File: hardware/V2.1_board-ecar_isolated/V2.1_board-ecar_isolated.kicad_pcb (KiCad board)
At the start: 2 copper layers, 160 x 100 mm, 99 parts, among them IC1 ATMEGA8A-P, J1 2x BATT IN, J10 24V, J11 18V, J12 5V, J13 Analog-in-2 0-5V, J14 IGBT [GND, Gate], J15 Analog-in-3 - 30to5 (batt), J17 2x Switch (to 5V), J18 Relay contacts [NO, COM, NC], J19 2x 5V, J2 ST 2x GND, J20 ADC Battery, J21 ADC reserve, J22 ADC Gas-pedal, J23 2x 24V filtered, J24 Fan [GND-supp, Diode, Mosfet], J3 2x 24V filtered, J4 ST 2x GND, J5 PWM-Signal, J6 LED 3,2V 20mA [-, +], J7 Gas Pedal, J8 Gate, J9 BATT, K1 LEG-5, P1 ISP, Q1 BC547, Q2 IRFZ24N, Q3 BC547, U1 LM7818CT, U2 LM2576T-5, U3 TC429

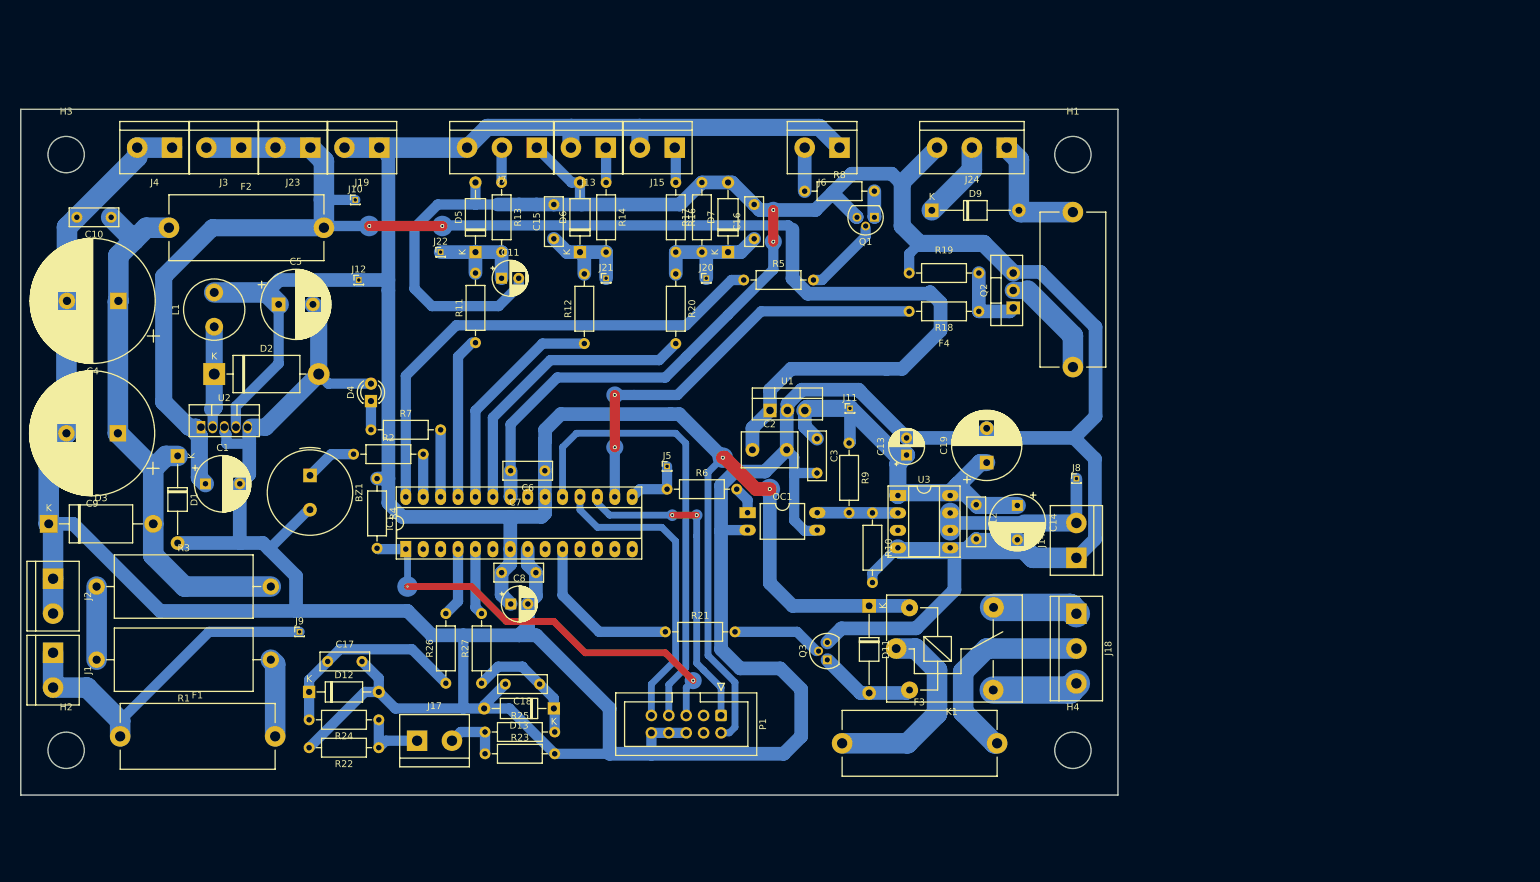
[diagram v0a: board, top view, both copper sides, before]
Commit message: pcb: small additions, begin footprint placment
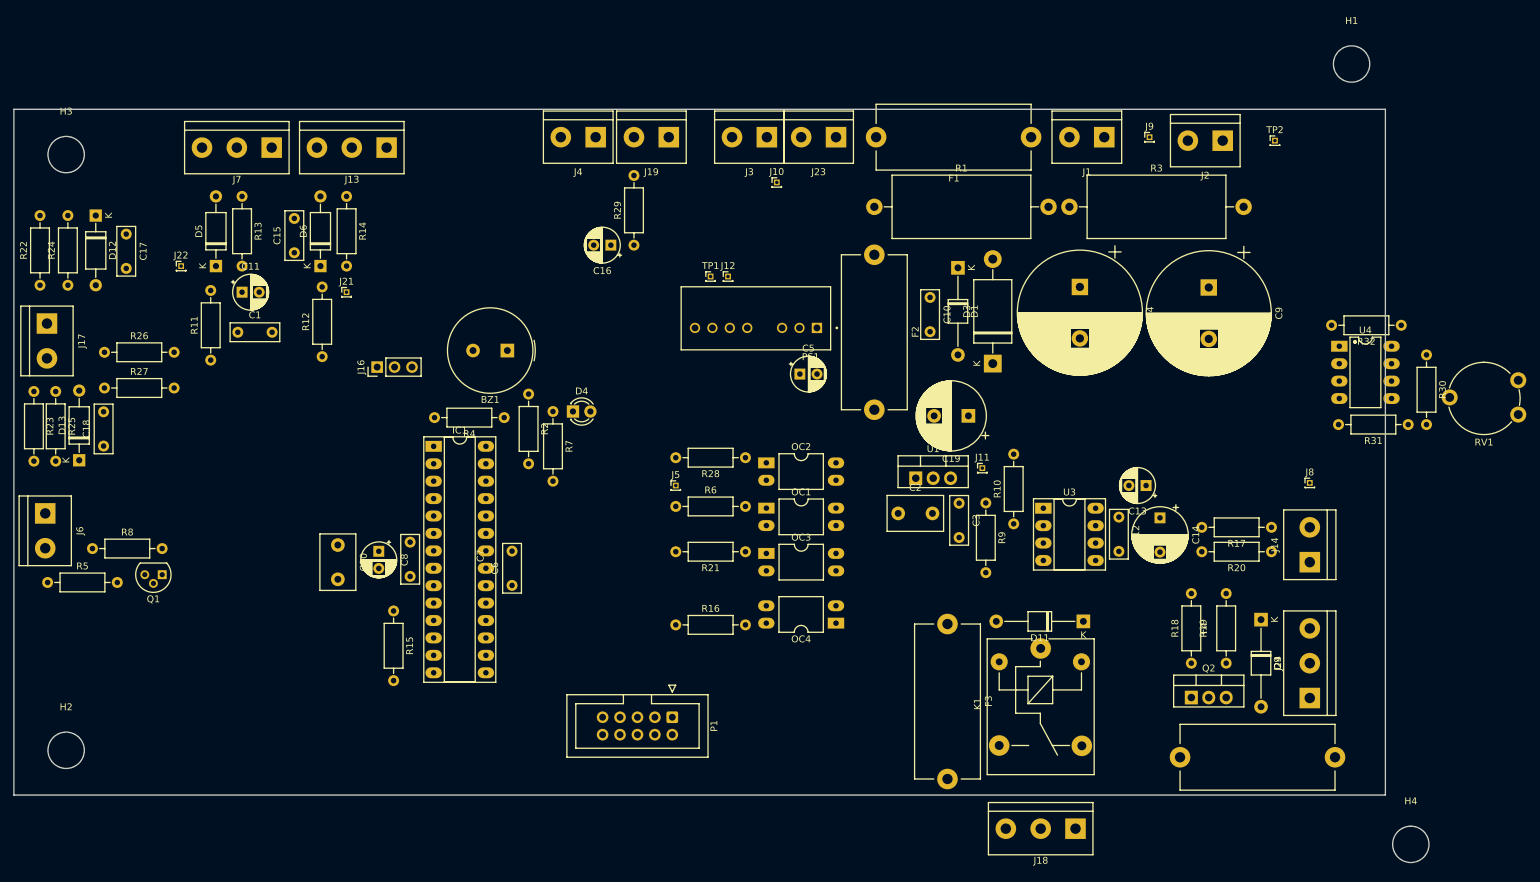
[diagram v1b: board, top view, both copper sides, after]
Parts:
- removed D2: 1N5822, Diode_THT:D_DO-201AD_P15.24mm_Horizontal
- removed D7: 5V1, Diode_THT:D_A-405_P10.16mm_Horizontal
- removed J15: Analog-in-3 - 30to5 (batt), TerminalBlock:TerminalBlock_bornier-2_P5.08mm
- removed J20: ADC Battery, Connector_PinHeader_1.00mm:PinHeader_1x01_P1.00mm_Vertical
- removed L1: 100u, Inductor_THT:L_Radial_D8.7mm_P5.00mm_Fastron_07HCP
- removed Q3: BC547, Package_TO_SOT_THT:TO-92L
- removed U2: LM2576T-5, Package_TO_SOT_THT:TO-220-5_Vertical
- added C20: 330nF, Capacitor_THT:C_Disc_D8.0mm_W5.0mm_P5.00mm, F.Cu at (47.2, 63.5)
- added J16: UART [TX, RX, GND], Connector_PinHeader_2.54mm:PinHeader_1x03_P2.54mm_Vertical, F.Cu at (53.0, 37.6)
- added OC2: LTV-817, Package_DIP:DIP-4_W10.16mm_LongPads, F.Cu at (109.7, 51.6)
- added OC3: LTV-817, Package_DIP:DIP-4_W10.16mm_LongPads, F.Cu at (109.7, 64.8)
- added OC4: LTV-817, Package_DIP:DIP-4_W10.16mm_LongPads, F.Cu at (119.9, 74.9)
- added PS1: RSO-2405S, RSO-2405S:CONV_RSO-2405S, F.Cu at (108.2, 30.5)
- added R15: 330, Resistor_THT:R_Axial_DIN0207_L6.3mm_D2.5mm_P10.16mm_Horizontal, F.Cu at (55.4, 73.2)
- added R28: 200, Resistor_THT:R_Axial_DIN0207_L6.3mm_D2.5mm_P10.16mm_Horizontal, F.Cu at (106.7, 50.8)
- added R29: 20, Resistor_THT:R_Axial_DIN0207_L6.3mm_D2.5mm_P10.16mm_Horizontal, F.Cu at (90.4, 19.8)
- added R30: 150k, Resistor_THT:R_Axial_DIN0207_L6.3mm_D2.5mm_P10.16mm_Horizontal, F.Cu at (206.0, 35.8)
- added R31: 100k, Resistor_THT:R_Axial_DIN0207_L6.3mm_D2.5mm_P10.16mm_Horizontal, F.Cu at (203.3, 46.0)
- added R32: 1k, Resistor_THT:R_Axial_DIN0207_L6.3mm_D2.5mm_P10.16mm_Horizontal, F.Cu at (202.3, 31.5)
- added RV1: 500k, Potentiometer_THT:Potentiometer_Piher_PT-10-V10_Vertical, F.Cu at (219.4, 39.5)
- added TP1: GNDD, Connector_PinHeader_1.00mm:PinHeader_1x01_P1.00mm_Vertical, F.Cu at (101.6, 24.4)
- added TP2: GND-power, Connector_PinHeader_1.00mm:PinHeader_1x01_P1.00mm_Vertical, F.Cu at (183.9, 4.57)
- added U4: LM358N, Package_DIP_AKL:DIP-8_W7.62mm_LongPads, F.Cu at (193.3, 34.6)
- C1: value 100u -> 100n; footprint Capacitor_THT:CP_Radial_D8.0mm_P5.00mm -> Capacitor_THT:C_Disc_D7.0mm_W2.5mm_P5.00mm
- C16: value 100n -> 10uf; footprint Capacitor_THT:C_Disc_D7.0mm_W2.5mm_P5.00mm -> Capacitor_THT:CP_Radial_D5.0mm_P2.50mm
- C5: value 1000u -> 10uf; footprint Capacitor_THT:CP_Radial_D10.0mm_P5.00mm -> Capacitor_THT:CP_Radial_D5.0mm_P2.50mm
- J13: value Analog-in-2 0-5V -> ADC reserve; footprint TerminalBlock:TerminalBlock_bornier-2_P5.08mm -> TerminalBlock:TerminalBlock_bornier-3_P5.08mm
- J19: value 2x 5V -> 5V, 5V-decoupled
- J2: value ST 2x GND -> ST 2x GND power
- J4: value ST 2x GND -> ST 2x GND 5V
- K1: value LEG-5 -> 24V relay
- R16: value 100k -> 10k
- R17: value 22k -> 0
- R18: value 1k -> 10k
- R19: value 22k -> 10k
- R20: value 2k2 -> nopop
- R21: value 470 -> 200
- R6: value 320 -> 200
- moved J2 182.1 mm to (176.3, 4.57), turned to 180 degrees
- moved J1 170.7 mm to (159.0, 4.06), turned to 180 degrees
- moved C9 160.5 mm to (174.2, 26.0), turned to -90 degrees
- moved F1 159.0 mm to (148.3, 4.06), turned to 180 degrees
- moved R3 152.3 mm to (153.9, 14.2)
- moved J9 143.4 mm to (165.6, 4.06)
- moved C4 140.2 mm to (155.4, 25.9), turned to -90 degrees
- moved D3 139.6 mm to (142.7, 37.1), turned to 90 degrees
- moved J6 127.5 mm to (4.57, 58.9), turned to -90 degrees
- moved C10 120.0 mm to (133.6, 27.4), turned to -90 degrees
- moved D1 117.1 mm to (137.7, 23.1)
- moved Q1 116.2 mm to (21.6, 67.9)
- moved R8 116.2 mm to (11.5, 64.1)
- moved R5 110.7 mm to (4.92, 69.0)
- moved R1 110.0 mm to (125.5, 14.2), turned to 0 degrees
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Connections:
- C1 pad 1: +24V filtered -> Net-(D5-K)
- C10 pad 2: GND -> GNDPWR
- C12 pad 2: GND -> GNDPWR
- C13 pad 2: GND -> GNDPWR
- C14 pad 2: GND -> GNDPWR
- C16 pad 1: Net-(D7-K) -> +5V
- C19 pad 2: GND -> GNDPWR
- C2 pad 2: GND -> GNDPWR
- C3 pad 2: GND -> GNDPWR
- C4 pad 2: GND -> GNDPWR
- C5 pad 1: +5V -> +24V filtered
- C5 pad 2: GND -> GNDPWR
- C9 pad 2: GND -> GNDPWR
- D1 pad 2: GND -> GNDPWR
- D11 pad 1: +5V -> +24V filtered
- D3 pad 1: GND -> GNDPWR
- IC1 pad 2: unconnected-(IC1-(RXD)PD0-Pad2) -> /UART_RX
- IC1 pad 23: /analog2 (30V Batt) -> /battery-threshold
- IC1 pad 3: unconnected-(IC1-(TXD)PD1-Pad3) -> /UART_TX
- IC1 pad 9: unconnected-(IC1-PB6(XTAL1/TOSC1)-Pad9) -> Net-(IC1-PB6(XTAL1/TOSC1))
- J13 pad 1: Net-(J13-Pin_1) -> GND
- J13 pad 2: +5V -> Net-(J13-Pin_2)
- J14 pad 1: GND -> GNDPWR
- J19 pad 2: +5V -> Net-(J19-Pin_2)
- J2 pad 1: GND -> GNDPWR
- J2 pad 2: GND -> GNDPWR
- J24 pad 3: GND -> GNDPWR
- K1 pad 5: +5V -> +24V filtered
- OC1 pad 3: GND -> GNDPWR
- P1 pad 4: unconnected-(P1-Pad4) -> GND
- Q2 pad 3: GND -> GNDPWR
- R10 pad 2: GND -> GNDPWR
- R14 pad 1: Net-(J13-Pin_1) -> Net-(J13-Pin_2)
- R16 pad 1: Net-(J15-Pin_1) -> +5V
- R16 pad 2: Net-(D7-K) -> /battery-threshold
- R17 pad 1: Net-(D7-K) -> Net-(J14-Pin_2)
- R17 pad 2: GND -> Net-(R17-Pad2)
- R18 pad 2: /Mosfet (fan) -> +24V filtered
- R19 pad 1: GND -> GNDPWR
- R20 pad 1: Net-(D7-K) -> Net-(J14-Pin_2)
- R20 pad 2: /analog2 (30V Batt) -> Net-(R17-Pad2)
- R21 pad 1: /Relay (light) -> Net-(OC3-Pad1)
- R21 pad 2: Net-(Q3-B) -> /Relay (light)
- U1 pad 2: GND -> GNDPWR
- U3 pad 4: GND -> GNDPWR
- U3 pad 5: GND -> GNDPWR
- U3 pad 6: Net-(J14-Pin_2) -> Net-(R17-Pad2)
- U3 pad 7: Net-(J14-Pin_2) -> Net-(R17-Pad2)
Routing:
- net GND: track 888.8 -> 0.00 mm, vias 2 -> 0
- net +5V: track 353.0 -> 0.00 mm, vias 2 -> 0
- net +24V filtered: track 233.3 -> 0.00 mm, vias 2 -> 0
- net Net-(D1-K): track 83.0 -> 0.00 mm
- net /LED-ext: track 72.7 -> 0.00 mm
- net +18V: track 69.5 -> 0.00 mm
- net /SCK: track 67.4 -> 0.00 mm
- net /Mosfet (fan): track 62.8 -> 0.00 mm, vias 2 -> 0
- net /RESET: track 62.6 -> 0.00 mm, vias 2 -> 0
- net +BATT: track 50.7 -> 0.00 mm
- net /MOSI: track 46.8 -> 0.00 mm, vias 2 -> 0
- net /MISO: track 44.6 -> 0.00 mm
- net /analog2 (30V Batt): track 42.7 -> 0.00 mm
- net /analog1: track 32.5 -> 0.00 mm
- net Net-(J18-Pin_2): track 30.6 -> 0.00 mm
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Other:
- board size 160 x 100 mm -> 200 x 100 mm
- board text removed: "Analog_0-30V (Pin-23/PC0) 5V(out), 24V(in)"

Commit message: pcb: optimize placement, assignment
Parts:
- removed F2: 500mA, Fuse:Fuseholder_Cylinder-5x20mm_Stelvio-Kontek_PTF78_Horizontal_Open
- removed J22: ADC Gas-pedal, Connector_PinHeader_1.00mm:PinHeader_1x01_P1.00mm_Vertical
- removed J3: 2x 24V filtered, TerminalBlock:TerminalBlock_bornier-2_P5.08mm
- added C21: 100n, Capacitor_THT:C_Disc_D7.0mm_W2.5mm_P5.00mm, F.Cu at (118.9, 45.8)
- added TP3: DRV-in, Connector_PinHeader_1.00mm:PinHeader_1x01_P1.00mm_Vertical, F.Cu at (120.9, 57.9)
- added TP4: GP-in, Connector_PinHeader_1.00mm:PinHeader_1x01_P1.00mm_Vertical, F.Cu at (13.7, 12.2)
- added TP5: GP-filtered, Connector_PinHeader_1.00mm:PinHeader_1x01_P1.00mm_Vertical, F.Cu at (16.3, 26.9)
- R24, R25: value 10k -> 47k
- moved R30 130.2 mm to (85.0, 84.0)
- moved R31 130.2 mm to (82.3, 94.1)
- moved U4 130.2 mm to (72.3, 82.7)
- moved RV1 128.7 mm to (99.5, 86.2)
- moved R32 127.8 mm to (83.7, 79.1), turned to 0 degrees
- moved P1 85.2 mm to (48.8, 17.8)
- moved D4 78.0 mm to (38.6, 109.2), turned to 180 degrees
- moved R7 70.5 mm to (41.7, 104.1), turned to 180 degrees
- moved BZ1 61.5 mm to (40.3, 87.9), turned to 0 degrees
- moved R2 53.0 mm to (34.5, 75.7), turned to 90 degrees
- moved C6 43.6 mm to (34.8, 47.8), turned to -90 degrees
- moved C13 39.9 mm to (128.2, 39.6)
- moved R20 38.3 mm to (145.8, 57.4), turned to 90 degrees
- moved C4 37.9 mm to (117.6, 26.5)
- moved C9 37.6 mm to (136.7, 26.5)
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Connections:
- C10 pad 1: Net-(D1-K) -> +24V filtered
- C4 pad 1: Net-(D1-K) -> +24V filtered
- C9 pad 1: Net-(D1-K) -> +24V filtered
- D1 pad 1: Net-(D1-K) -> +24V filtered
- D3 pad 2: Net-(D1-K) -> +24V filtered
- IC1 pad 10: /Relay (light) -> unconnected-(IC1-PB7(XTAL2/TOSC2)-Pad10)
- IC1 pad 16: /Mosfet (fan) -> /LED
- IC1 pad 23: /battery-threshold -> /analog1
- IC1 pad 24: /analog1 -> /analog0 (gas)
- IC1 pad 25: /analog0 (gas) -> /Switch1
- IC1 pad 26: /LED -> /Switch2
- IC1 pad 4: /Switch1 -> /battery-threshold
- IC1 pad 5: /Switch2 -> /Relay (light)
- IC1 pad 6: unconnected-(IC1-(XCK/T0)PD4-Pad6) -> /Mosfet (fan)
- R3 pad 2: Net-(D1-K) -> +24V filtered
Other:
- board size 200 x 100 mm -> 160 x 100 mm

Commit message: pcb: routing, pre gnd-plane
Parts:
- added R33: 2k2, Resistor_THT:R_Axial_DIN0207_L6.3mm_D2.5mm_P10.16mm_Horizontal, F.Cu at (63.5, 71.5)
- J13: value ADC reserve -> ADC reserve [5V, in, GND]
- J14: value IGBT [GND, Gate] -> IGBT [Gate, GND]
- J17: value 2x Switch (to 5V) -> 2x Switch (to 5V) [PC3, PC2]
- J19: value 5V, 5V-decoupled -> [5V, 5V-decoupled]
- J24: value Fan [GND-supp, Diode, Mosfet] -> Fan [GND/Mosfet-OUT, Diode, 24V-filtered]
- J4: value ST 2x GND 5V -> 2x GND (5V)
- J7: value Gas Pedal -> Gas Pedal [5V, In, GND]
- moved H2 104.5 mm to (61.6, 31.7)
- moved H3 102.0 mm to (8.03, 92.1)
- moved J6 89.9 mm to (47.2, 5.21), turned to 180 degrees
- moved R8 88.6 mm to (36.6, 5.59), turned to -90 degrees
- moved Q1 75.3 mm to (40.1, 13.2)
- moved R5 39.7 mm to (32.5, 33.8), turned to 90 degrees
- moved TP2 39.7 mm to (147.2, 43.0)
- moved H1 33.3 mm to (202.5, 25.9)
- moved H4 32.0 mm to (153.5, 96.2)
- moved R7 30.9 mm to (29.6, 75.7), turned to 90 degrees
- moved R11 30.6 mm to (27.6, 57.9)
- moved D4 22.5 mm to (29.6, 88.6), turned to 0 degrees
- moved R12 21.4 mm to (30.9, 55.4)
- moved J8 21.0 mm to (138.7, 56.4)
- moved R27 10.1 mm to (24.3, 73.2), turned to 90 degrees
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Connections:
- IC1 pad 16: /LED -> /LED-ext
- IC1 pad 27: /BUZZER -> /LED
- IC1 pad 28: /LED-ext -> /BUZZER
- J14 pad 1: GNDPWR -> Net-(J14-Pin_1)
- J14 pad 2: Net-(J14-Pin_2) -> GNDPWR
- J24 pad 3: GNDPWR -> +24V filtered
- J8 pad 1: Net-(J14-Pin_2) -> Net-(J14-Pin_1)
- OC4 pad 4: /battery-threshold -> Net-(OC4-Pad4)
- R16 pad 2: /battery-threshold -> Net-(OC4-Pad4)
- R17 pad 1: Net-(J14-Pin_2) -> Net-(J14-Pin_1)
- R20 pad 1: Net-(J14-Pin_2) -> Net-(J14-Pin_1)
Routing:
- net +24V filtered: track 0.00 -> 329.7 mm
- net +5V: track 0.00 -> 224.8 mm
- net GNDPWR: track 0.00 -> 214.8 mm, vias 0 -> 4
- net GND: track 0.00 -> 152.6 mm, vias 0 -> 9
- net +18V: track 0.00 -> 118.5 mm, vias 0 -> 2
- net (no net): track 0.00 -> 115.5 mm
- net Net-(Q2-G): track 0.00 -> 85.5 mm
- net Net-(U3-INPUT): track 0.00 -> 69.8 mm
- net /RESET: track 0.00 -> 61.1 mm, vias 0 -> 2
- net /SCK: track 0.00 -> 46.2 mm
- net /MISO: track 0.00 -> 43.6 mm
- net Net-(D5-K): track 0.00 -> 40.2 mm
- net /PWM_0: track 0.00 -> 37.5 mm
- net /MOSI: track 0.00 -> 37.0 mm, vias 0 -> 2
- net Net-(D11-A): track 0.00 -> 35.8 mm
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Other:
- copper layers 2 -> 4
- board text removed: "2x Switch to 5V (Pin-4 / PD2), (Pin-5 / PD3)"
- board text removed: "Analog_0-5V (Pin-24/PC1) 5V, A(in)"
- board text removed: "Analog_gas (Pin-25/PC2) 5V, Pedal, GND"
- board text removed: "FUSE 24V Filtered"
- board text removed: "Fan GND(in/out), Fan+(in), Fan-(out) (Pin-16/PB2)"
- board text removed: "GND, Gate IGBT (Pin-16/PB2)"

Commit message: pcb: gnd-planes, testpoints, optimize, pcb2gcode - milling
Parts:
- added TP10: SW-filtered, Connector_PinHeader_1.00mm:PinHeader_1x01_P1.00mm_Vertical, F.Cu at (21.8, 45.5)
- added TP11: SW-in, Connector_PinHeader_1.00mm:PinHeader_1x01_P1.00mm_Vertical, F.Cu at (11.9, 58.2)
- added TP6: BATT, Connector_PinHeader_1.00mm:PinHeader_1x01_P1.00mm_Vertical, F.Cu at (97.5, 13.7)
- added TP7: OP -, Connector_PinHeader_1.00mm:PinHeader_1x01_P1.00mm_Vertical, F.Cu at (84.2, 96.9)
- added TP8: OP +, Connector_PinHeader_1.00mm:PinHeader_1x01_P1.00mm_Vertical, F.Cu at (90.0, 96.9)
- added TP9: OP out, Connector_PinHeader_1.00mm:PinHeader_1x01_P1.00mm_Vertical, F.Cu at (88.0, 75.0)
- J9: value BATT -> BATT-F
- moved H1 209.2 mm to (5.00, 95.0)
- moved H2 112.9 mm to (155.0, 95.0)
- moved H3 94.7 mm to (63.0, 15.0)
- moved H4 91.2 mm to (155.0, 5.00)
- moved J9 14.2 mm to (128.5, 11.4)
- moved J2 7.52 mm to (145.8, 4.83)
- moved C16 2.06 mm to (73.7, 20.4)
- moved J1 0.80 mm to (134.4, 4.83)
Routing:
- net (no net): track 115.5 -> 0.00 mm
- net GNDPWR: track 214.8 -> 116.6 mm, vias 4 -> 6
- net +5V: track 224.8 -> 238.6 mm
- net Net-(Q2-D): track 1.22 -> 13.7 mm
- net Net-(U4B-+): track 10.2 -> 17.7 mm
- net Net-(D9-A): track 8.59 -> 15.2 mm
- net +BATT: track 10.8 -> 17.0 mm
- net Net-(J17-Pin_1): track 9.86 -> 15.9 mm
- net Net-(F1-Pad2): track 10.3 -> 14.8 mm
- net Net-(U4B--): track 15.6 -> 18.4 mm
- net GND: track 152.6 -> 150.1 mm
- net /PWM_0: track 37.5 -> 36.6 mm
- net Net-(D6-K): track 33.2 -> 34.0 mm
- net /SCK: track 46.2 -> 46.7 mm
- added copper zone on B.Cu, net GND
- added copper zone on F.Cu, net GND
- added copper zone on B.Cu, net GNDPWR
- added copper zone on F.Cu, net GNDPWR
